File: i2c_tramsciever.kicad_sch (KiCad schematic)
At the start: 6 parts, among them U2 PCA9306DP

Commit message: Fix decimal point connection on ds4, add info to title block
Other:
- company: (none) -> Andrew Tudoroi
- title: (none) -> Pitanga HAT
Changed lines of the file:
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@@
 (kicad_sch (version 20230121) (generator eeschema)
   (paper "A4")
+  (title_block
+    (title "Pitanga HAT")
+    (date "2023-10-19")
+    (rev "2.1")
+    (company "Andrew Tudoroi")
+  )
   (junction (at 146.05 72.39) (diameter 0) (color 0 0 0 0)
   )

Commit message: Piatnag_5_bt
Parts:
- C11: footprint Capacitor_SMD:C_0402_1005Metric -> Capacitor_SMD:C_0603_1608Metric
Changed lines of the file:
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@@
       (project "ltp_kikad"
         (path "/eed35b77-cbf9-4596-9b17-2558f81058ba/e885c20e-c513-4e27-ac27-692e5f196b61"
-          (reference "R20") (unit 1)
+          (reference "R18") (unit 1)
         )
       )
@@
       (effects (font (size 1.27 1.27)) (justify left))
     )
-    (property "Footprint" "Capacitor_SMD:C_0402_1005Metric" (at 171.45 68.58 0)
+    (property "Footprint" "Capacitor_SMD:C_0603_1608Metric" (at 171.45 68.58 0)
       (effects (font (size 1.27 1.27)) hide)
     )
@@
         )
         (path "/eed35b77-cbf9-4596-9b17-2558f81058ba/e885c20e-c513-4e27-ac27-692e5f196b61"
-          (reference "C16") (unit 1)
+          (reference "C12") (unit 1)
         )
       )
@@
       (project "ltp_kikad"
         (path "/eed35b77-cbf9-4596-9b17-2558f81058ba/e885c20e-c513-4e27-ac27-692e5f196b61"
-          (reference "U2") (unit 1)
+          (reference "U1") (unit 1)
         )
       )
@@
         )
         (path "/eed35b77-cbf9-4596-9b17-2558f81058ba/e885c20e-c513-4e27-ac27-692e5f196b61"
-          (reference "#PWR044") (unit 1)
+          (reference "#PWR039") (unit 1)
         )
       )
@@
         )
         (path "/eed35b77-cbf9-4596-9b17-2558f81058ba/e885c20e-c513-4e27-ac27-692e5f196b61"
-          (reference "#PWR043") (unit 1)
+          (reference "#PWR035") (unit 1)
         )
       )
@@
       (project "ltp_kikad"
         (path "/eed35b77-cbf9-4596-9b17-2558f81058ba/e885c20e-c513-4e27-ac27-692e5f196b61"
-          (reference "R18") (unit 1)
+          (reference "R16") (unit 1)
         )
       )
@@
       (effects (font (size 1.27 1.27)) (justify left))
     )
-    (property "Footprint" "Capacitor_SMD:C_0402_1005Metric" (at 119.38 73.66 0)
+    (property "Footprint" "Capacitor_SMD:C_0603_1608Metric" (at 119.38 73.66 0)
       (effects (font (size 1.27 1.27)) hide)
     )
@@
         )
         (path "/eed35b77-cbf9-4596-9b17-2558f81058ba/e885c20e-c513-4e27-ac27-692e5f196b61"
-          (reference "C15") (unit 1)
+          (reference "C11") (unit 1)
         )
       )
@@
       (project "ltp_kikad"
         (path "/eed35b77-cbf9-4596-9b17-2558f81058ba/e885c20e-c513-4e27-ac27-692e5f196b61"
-          (reference "R19") (unit 1)
+          (reference "R17") (unit 1)
         )
       )
@@
       (project "ltp_kikad"
         (path "/eed35b77-cbf9-4596-9b17-2558f81058ba/e885c20e-c513-4e27-ac27-692e5f196b61"
-          (reference "#PWR046") (unit 1)
+          (reference "#PWR038") (unit 1)
         )
       )
@@
       (project "ltp_kikad"
         (path "/eed35b77-cbf9-4596-9b17-2558f81058ba/e885c20e-c513-4e27-ac27-692e5f196b61"
-          (reference "#PWR045") (unit 1)
+          (reference "#PWR037") (unit 1)
         )
       )
@@
         )
         (path "/eed35b77-cbf9-4596-9b17-2558f81058ba/e885c20e-c513-4e27-ac27-692e5f196b61"
-          (reference "#PWR042") (unit 1)
-        )
-      )
+          (reference "#PWR036") (unit 1)
+        )
+      )

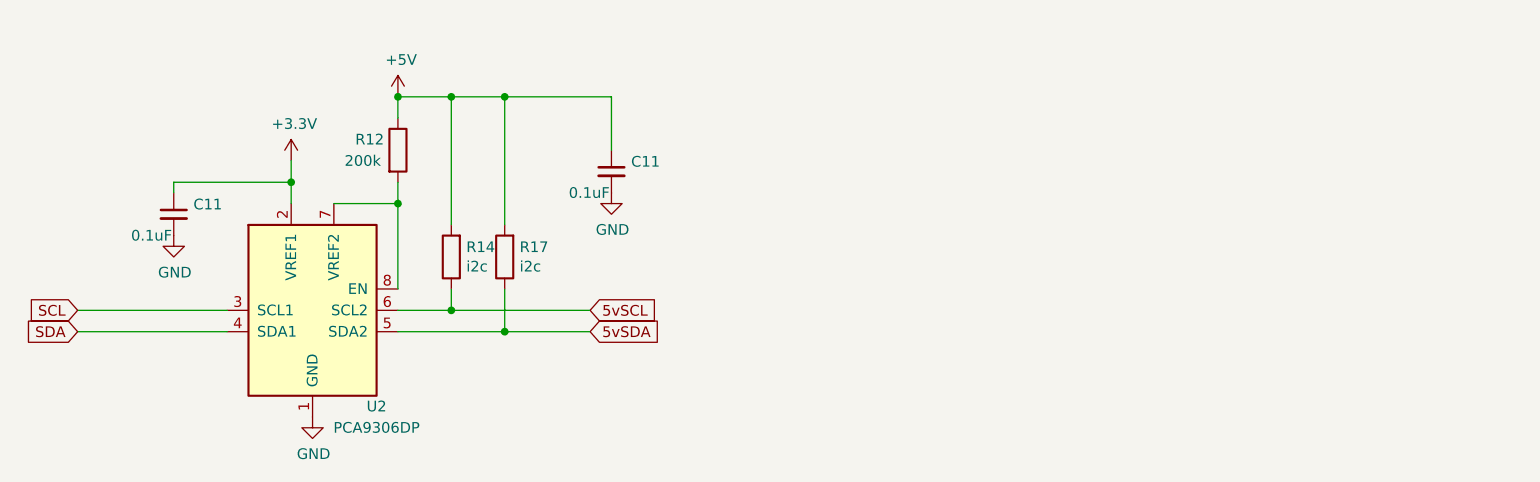
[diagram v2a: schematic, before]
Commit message: Move from 4 layer to 2, complete roting, separate 5v for led driver and 3v i2c power
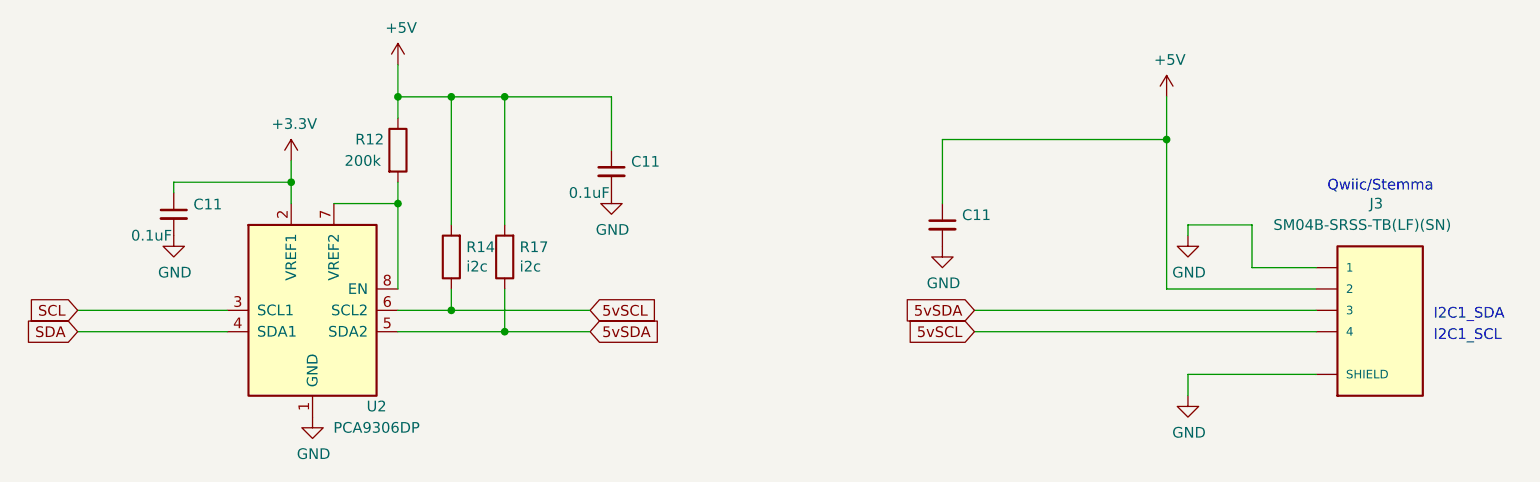
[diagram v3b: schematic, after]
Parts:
- added C11: 10uF, Capacitor_SMD:C_0603_1608Metric, symbol Device:C_Small
- added J3: SM04B-SRSS-TB(LF)(SN), ltp_kikad:JST_SM04B-SRSS-TB(LF)(SN), symbol SM04B-SRSS-TB_LF__SN_:SM04B-SRSS-TB(LF)(SN)
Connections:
- net +5V: now also C11.1, J3.2
- net 5vSCL: now also J3.4
- net 5vSDA: now also J3.3
- net GND: now also C11.2, J3.1, J3.S1 (SHIELD), J3.S2 (SHIELD)
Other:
- note added: "I2C1_SCL"
- note added: "I2C1_SDA"
- note added: "Qwiic/Stemma"
